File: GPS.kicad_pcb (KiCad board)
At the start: 2 copper layers, 80.5 x 80.5 mm, 48 parts, among them J101 USB_B_Micro, J102 Conn_01x05, J103 Conn_01x10, U101 AP7361C-10E, U102 AZ1117-3.3, U103 AZ1117-3.3, U104 SMA_CONN, U105 M10578-A2, U106 MCP2562-H-SN, U107 STM32F103C8T6, Y101 8MHz

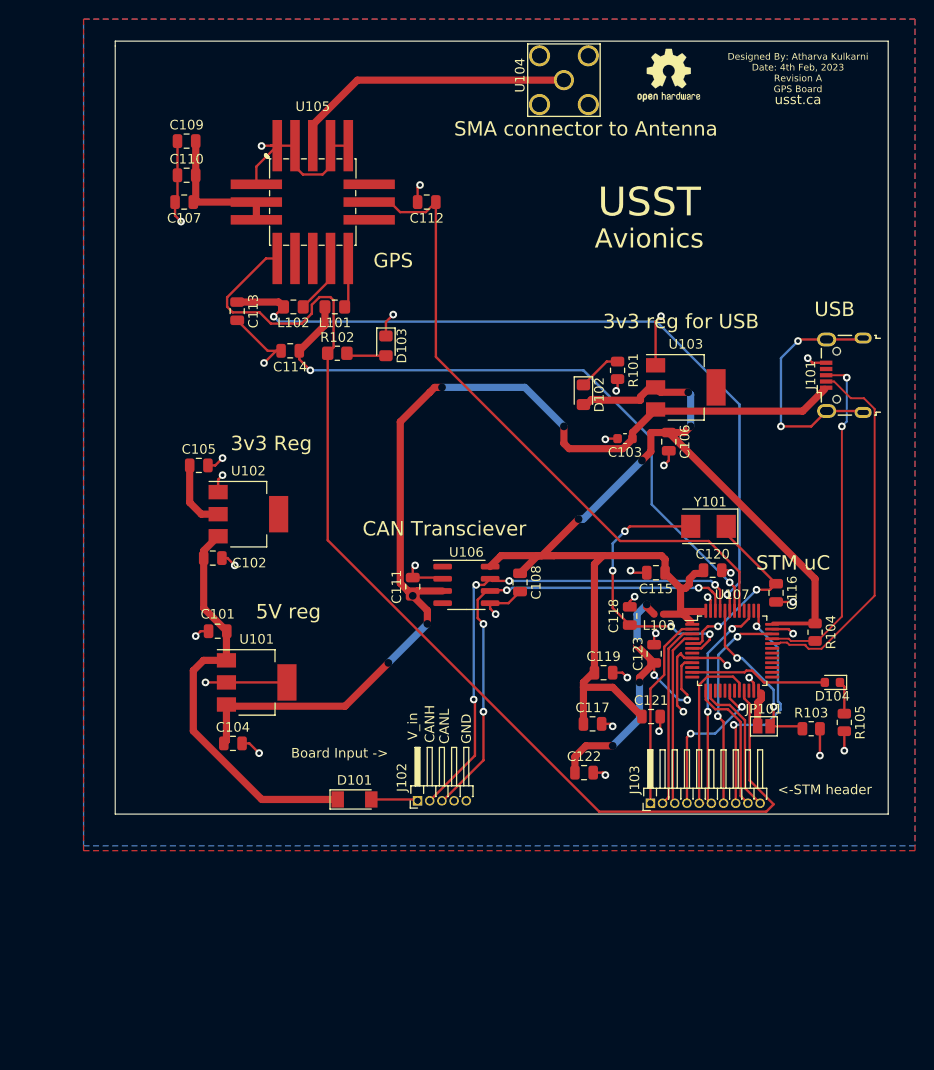
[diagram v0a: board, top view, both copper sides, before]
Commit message: Add files via upload
Updated PCB layout with proper RF traces and differential pairs. PCB dimensions are now 70 mm by 70 mm
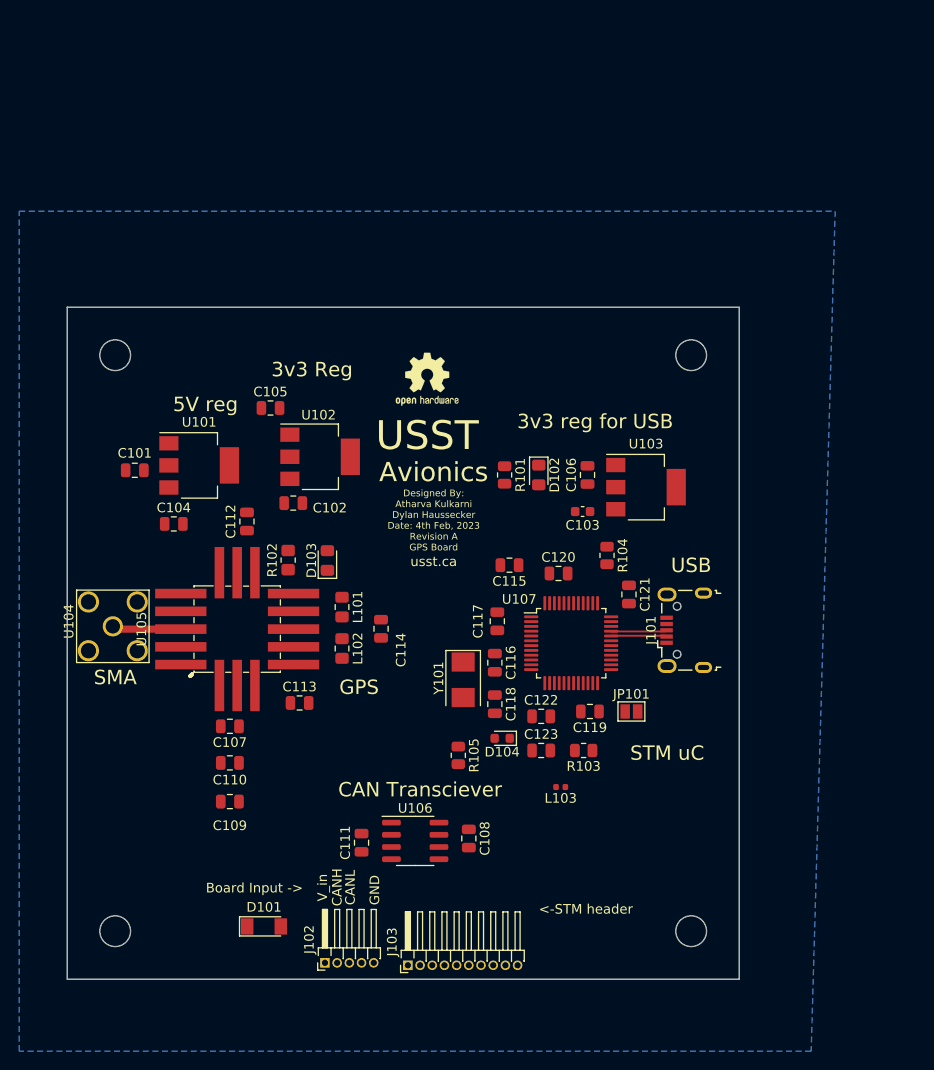
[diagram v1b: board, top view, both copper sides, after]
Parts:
- added H1: MountingHole, MountingHole:MountingHole_3.2mm_M3, F.Cu at (127.5, 82.5)
- added H2: MountingHole, MountingHole:MountingHole_3.2mm_M3, F.Cu at (127.5, 142.5)
- added H3: MountingHole, MountingHole:MountingHole_3.2mm_M3, F.Cu at (187.5, 142.5)
- added H4: MountingHole, MountingHole:MountingHole_3.2mm_M3, F.Cu at (187.5, 82.5)
- moved U104 73.8 mm to (127.3, 110.7)
- moved C109 68.9 mm to (139.4, 129.0)
- moved C110 61.4 mm to (139.4, 125.0)
- moved C107 54.8 mm to (139.4, 121.2)
- moved U105 45.2 mm to (140.2, 111.0), turned to 90 degrees
- moved C113 41.3 mm to (146.7, 118.7), turned to 0 degrees
- moved REF** 40.4 mm to (160.0, 85.0)
- moved R105 40.4 mm to (163.2, 124.2)
- moved C112 38.2 mm to (141.2, 99.8), turned to 90 degrees
- moved L102 35.9 mm to (151.1, 113.1), turned to -90 degrees
- moved D104 34.9 mm to (167.8, 122.4)
- moved J101 31.3 mm to (186.8, 111.2)
- moved L101 31.3 mm to (151.1, 108.7), turned to -90 degrees
- moved C114 30.5 mm to (155.2, 111.0), turned to -90 degrees
- moved J103 30.4 mm to (158.0, 146.1)
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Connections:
- D101 pad 2: Net-(D101-Pad2) -> unconnected-(D101-Pad2)
- J102 pad 1: Net-(D101-Pad2) -> unconnected-(J102-Pad1)
- J102 pad 2: /CANH -> unconnected-(J102-Pad2)
- J102 pad 3: /CANL -> unconnected-(J102-Pad3)
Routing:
- net +3.3V: track 144.4 -> 0.00 mm, vias 4 -> 0
- net /FIX: track 120.5 -> 0.00 mm
- net GND: track 115.4 -> 0.00 mm, vias 34 -> 0
- net +5V: track 107.1 -> 0.00 mm, vias 5 -> 0
- net /STM_RX_GPS_TX: track 80.9 -> 0.00 mm, vias 2 -> 0
- net /~{HWR}: track 68.9 -> 0.00 mm
- net /STM_TX_GPS_RX: track 68.2 -> 0.00 mm, vias 2 -> 0
- net /CANH: track 52.9 -> 0.00 mm, vias 4 -> 0
- net /CANL: track 50.3 -> 0.00 mm, vias 4 -> 0
- net /V_in: track 42.7 -> 0.00 mm
- net +3.3VA: track 35.9 -> 0.00 mm, vias 6 -> 0
- net USB_D-: track 39.0 -> 5.63 mm
- net USB_D+: track 35.8 -> 5.63 mm, vias 2 -> 0
- net /HSE_IN: track 29.6 -> 0.00 mm, vias 4 -> 0
- net unconnected-(J101-Pad6): track 25.8 -> 0.00 mm, vias 2 -> 0
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- removed copper zone on F.Cu, net +3.3V
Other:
- board size 80.5 x 80.5 mm -> 70 x 70 mm
- board text added: "Designed By: Atharva Kulkarni Dylan Haussecker Date: 4th Feb, 2023 Revision A GPS Board"
- board text added: "SMA"
- board text removed: "Designed By: Atharva Kulkarni Date: 4th Feb, 2023 Revision A GPS Board"
- board text removed: "SMA connector to Antenna"

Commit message: made changes for CANH/L and added STM programming header
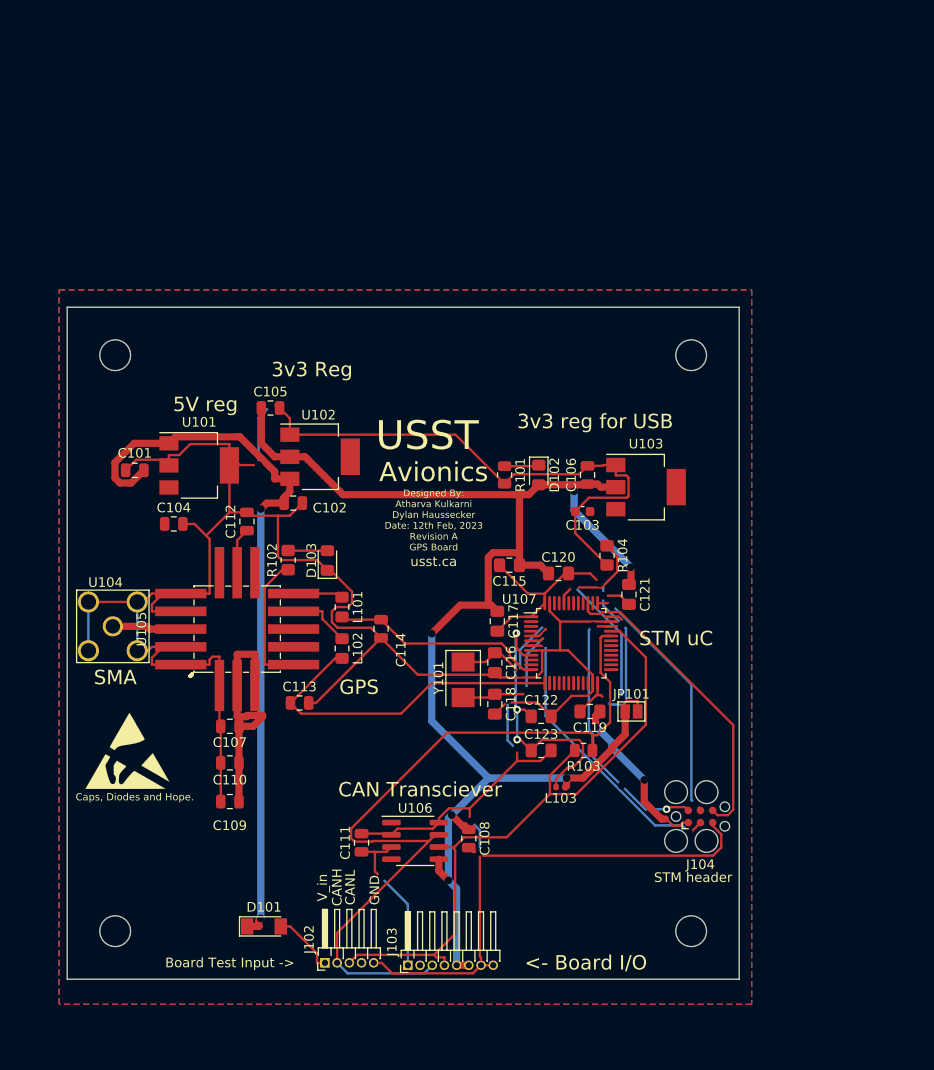
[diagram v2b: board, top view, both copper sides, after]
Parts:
- removed D104: BLUE, LED_SMD:LED_0603_1608Metric
- removed J101: USB_B_Micro, Connector_USB:USB_Micro-B_Wuerth_629105150521
- removed R105: 1k5, Resistor_SMD:R_0805_2012Metric
- removed the REF** at (160.0, 85.0)
- added J104: Conn_01x06_Female, Connector:Tag-Connect_TC2030-IDC-FP_2x03_P1.27mm_Vertical, F.Cu at (188.5, 130.6)
- added REF**: ESD-Logo_8.9x8mm_SilkScreen, Symbol:ESD-Logo_8.9x8mm_SilkScreen, F.Cu at (128.8, 123.7)
- C115, C116, C117, C118, C119, C120, C121, C122, C123: footprint Capacitor_SMD:C_0805_2012Metric -> Capacitor_SMD:C_0805_2012Metric_Pad1.18x1.45mm_HandSolder
- J103: value Conn_01x10 -> Conn_01x08_Female; footprint Connector_PinHeader_1.27mm:PinHeader_1x10_P1.27mm_Horizontal -> Connector_PinHeader_1.27mm:PinHeader_1x08_P1.27mm_Horizontal
- R103: value 10k -> 120
- R104: value 1k5 -> 10k; footprint Resistor_SMD:R_0805_2012Metric -> Resistor_SMD:R_0805_2012Metric_Pad1.20x1.40mm_HandSolder
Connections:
- C115 pad 2: GND -> Net-(C115-Pad2)
- C117 pad 2: GND -> Net-(C115-Pad2)
- C119 pad 2: GND -> Net-(C115-Pad2)
- C120 pad 2: GND -> Net-(C115-Pad2)
- C121 pad 2: GND -> Net-(C115-Pad2)
- D101 pad 2: unconnected-(D101-Pad2) -> Net-(D101-Pad2)
- J102 pad 1: unconnected-(J102-Pad1) -> Net-(D101-Pad2)
- J102 pad 2: unconnected-(J102-Pad2) -> /CANH
- J102 pad 3: unconnected-(J102-Pad3) -> /CANL
- J103 pad 1: PC13 -> +5V
- J103 pad 2: PC14 -> +5V
- J103 pad 3: PC15 -> /CANH
- J103 pad 4: PB0 -> /CANL
- J103 pad 5: PB2 -> +3.3V
- J103 pad 6: SWO -> +3.3V
- J103 pad 7: SWDIO -> GND
- J103 pad 8: SWCLK -> GND
- R103 pad 1: /BOOT0 -> /CANH
- R103 pad 2: GND -> /CANL
- R104 pad 1: +3.3V -> /BOOT0
- R104 pad 2: USB_D+ -> GND
- U106 pad 5: GND -> +3.3V
- U106 pad 8: +3.3V -> GND
- U107 pad 1: +3.3V -> Net-(C115-Pad2)
- U107 pad 11: /LED_STAT -> unconnected-(U107-Pad11)
- U107 pad 12: unconnected-(U107-Pad12) -> /STM_TX_GPS_RX
- U107 pad 13: PA3 -> /STM_RX_GPS_TX
- U107 pad 14: PA4 -> unconnected-(U107-Pad14)
- U107 pad 15: PA5 -> unconnected-(U107-Pad15)
- U107 pad 16: PA6 -> unconnected-(U107-Pad16)
- U107 pad 17: PA7 -> unconnected-(U107-Pad17)
- U107 pad 18: PB0 -> unconnected-(U107-Pad18)
- U107 pad 19: PB1 -> unconnected-(U107-Pad19)
- U107 pad 2: PC13 -> unconnected-(U107-Pad2)
- U107 pad 20: PB2 -> unconnected-(U107-Pad20)
- U107 pad 21: /FIX -> unconnected-(U107-Pad21)
- U107 pad 24: +3.3V -> Net-(C115-Pad2)
- U107 pad 29: PA8 -> unconnected-(U107-Pad29)
- U107 pad 3: PC14 -> unconnected-(U107-Pad3)
- U107 pad 30: PA9 -> unconnected-(U107-Pad30)
- U107 pad 31: PA10 -> unconnected-(U107-Pad31)
- U107 pad 32: USB_D- -> /CANH
- U107 pad 33: USB_D+ -> /CANL
- U107 pad 34: SWDIO -> /SWDIO
- U107 pad 36: +3.3V -> Net-(C115-Pad2)
- U107 pad 37: SWCLK -> /SWCLK
- U107 pad 38: PA15 -> unconnected-(U107-Pad38)
- U107 pad 39: SWO -> /SWO
- U107 pad 4: PC15 -> unconnected-(U107-Pad4)
- U107 pad 41: /~{HWR} -> unconnected-(U107-Pad41)
- U107 pad 42: /STM_TX_GPS_RX -> unconnected-(U107-Pad42)
- U107 pad 43: /STM_RX_GPS_TX -> unconnected-(U107-Pad43)
- U107 pad 45: /CANH -> unconnected-(U107-Pad45)
- U107 pad 46: /CANL -> unconnected-(U107-Pad46)
- U107 pad 48: +3.3V -> Net-(C115-Pad2)
- U107 pad 7: unconnected-(U107-Pad7) -> /nRESET
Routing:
- net GND: track 0.00 -> 347.3 mm, vias 0 -> 6
- net +3.3V: track 0.00 -> 166.3 mm, vias 0 -> 8
- net /CANH: track 0.00 -> 81.7 mm
- net /V_in: track 0.00 -> 77.2 mm, vias 0 -> 2
- net /CANL: track 0.00 -> 67.6 mm
- net Net-(C115-Pad2): track 0.00 -> 45.7 mm, vias 0 -> 4
- net /STM_RX_GPS_TX: track 0.00 -> 35.6 mm
- net /SWO: track 0.00 -> 32.4 mm
- net /nRESET: track 0.00 -> 30.7 mm, vias 0 -> 2
- net +3.3VA: track 0.00 -> 30.3 mm, vias 0 -> 3
- net /SWDIO: track 0.00 -> 28.3 mm, vias 0 -> 3
- net /BOOT0: track 0.00 -> 27.3 mm, vias 0 -> 2
- net /SWCLK: track 0.00 -> 26.8 mm, vias 0 -> 2
- net +3V3: track 0.00 -> 25.1 mm
- net /STM_TX_GPS_RX: track 0.00 -> 22.2 mm
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- added copper zone on B.Cu, net +5V
- added copper zone on F.Cu, net +5V
- removed copper zone on B.Cu, net GND
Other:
- board text added: "<- Board I/O"
- board text added: "Board Test Input ->"
- board text added: "Caps, Diodes and Hope."
- board text added: "Designed By: Atharva Kulkarni Dylan Haussecker Date: 12th Feb, 2023 Revision A GPS Board"
- board text added: "STM header"
- board text removed: "<-STM header"
- board text removed: "Board Input ->"
- board text removed: "Designed By: Atharva Kulkarni Dylan Haussecker Date: 4th Feb, 2023 Revision A GPS Board"
- board text removed: "USB"
